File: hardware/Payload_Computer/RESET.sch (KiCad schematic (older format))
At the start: 2 parts

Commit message: More Library Updates
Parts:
- S?: symbol Payload_Computer-rescue:GPTS203211B-Symbols -> Symbols:GPTS203211B
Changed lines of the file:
@@
 $EndDescr
 $Comp
-L Payload_Computer-rescue:GPTS203211B-Symbols S?
+L Symbols:GPTS203211B S?
 U 1 1 5F8EA95B
 P 5350 3650

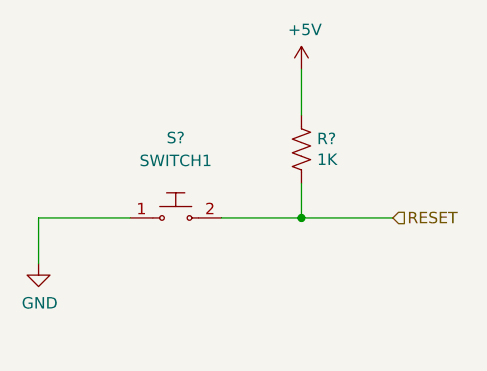
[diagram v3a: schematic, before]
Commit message: Updated processor for arduino. Fixed schematic a bit
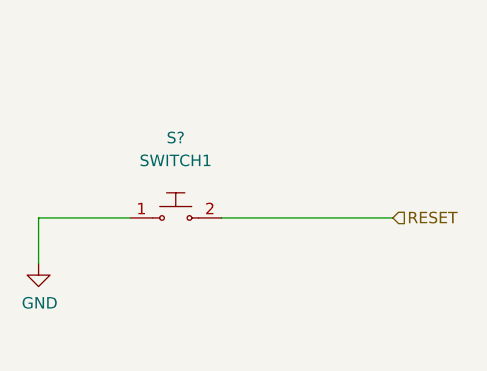
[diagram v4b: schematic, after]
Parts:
- removed R?: 1K, symbol Device:R_US
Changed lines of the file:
@@
 $Descr A4 11693 8268
 encoding utf-8
-Sheet 6 27
+Sheet 4 26
 Title ""
 Date ""
@@
 	1    0    0    -1
 $EndComp
-$Comp
-L Device:R_US R?
-U 1 1 5F8EC38D
-P 5900 3350
-F 0 "R?" H 5968 3396 50  0000 L CNN
-F 1 "1K" H 5968 3305 50  0000 L CNN
-F 2 "" V 5940 3340 50  0001 C CNN
-F 3 "~" H 5900 3350 50  0001 C CNN
-	1    5900 3350
-	1    0    0    -1
-$EndComp
-$Comp
-L power:+5V #PWR?
-U 1 1 5F8ECA21
-P 5900 3000
-F 0 "#PWR?" H 5900 2850 50  0001 C CNN
-F 1 "+5V" H 5915 3173 50  0000 C CNN
-F 2 "" H 5900 3000 50  0001 C CNN
-F 3 "" H 5900 3000 50  0001 C CNN
-	1    5900 3000
-	1    0    0    -1
-$EndComp
 Wire Wire Line
 	4750 3850 4750 3650
 Wire Wire Line
 	4750 3650 5150 3650
-Wire Wire Line
-	5550 3650 5900 3650
-Wire Wire Line
-	5900 3650 5900 3500
-Wire Wire Line
-	5900 3200 5900 3000
 Text HLabel 6300 3650 2    50   Input ~ 0
 RESET
 Wire Wire Line
-	6300 3650 5900 3650
-Connection ~ 5900 3650
+	5550 3650 6300 3650
 $EndSCHEMATC

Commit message: Finished Fan Schematic. Working on Servos
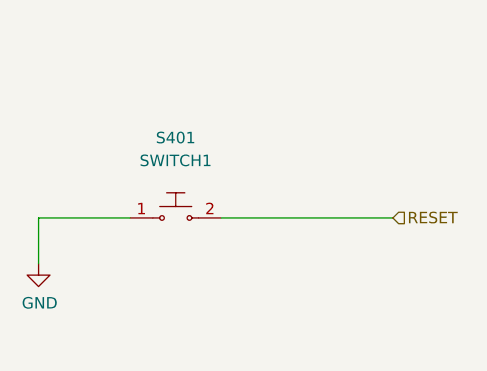
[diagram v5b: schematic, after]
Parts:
- gave numbers to parts that had none: 1
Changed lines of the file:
@@
 $Descr A4 11693 8268
 encoding utf-8
-Sheet 4 26
+Sheet 4 22
 Title ""
 Date ""
@@
 $EndDescr
 $Comp
-L Symbols:GPTS203211B S?
+L Symbols:GPTS203211B S401
 U 1 1 5F8EA95B
 P 5350 3650
-F 0 "S?" H 5350 4000 50  0000 C CNN
+F 0 "S401" H 5350 4000 50  0000 C CNN
 F 1 "SWITCH1" H 5350 3900 50  0000 C CNN
 F 2 "" H 5550 3850 50  0001 L CNN
@@
 $EndComp
 $Comp
-L power:GND #PWR?
+L power:GND #PWR0401
 U 1 1 5F8EBFC9
 P 4750 3850
-F 0 "#PWR?" H 4750 3600 50  0001 C CNN
+F 0 "#PWR0401" H 4750 3600 50  0001 C CNN
 F 1 "GND" H 4755 3677 50  0000 C CNN
 F 2 "" H 4750 3850 50  0001 C CNN
